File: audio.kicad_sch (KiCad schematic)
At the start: 109 parts, among them IC201 LC7881M, IC202 RC4560, IC203 RC4558, IC204 RC4558, J1 0, J2 0, Q201 2SC2412K, Q202 2SC2412K, Q203 DTA124EU3, Q204 DTA124EU3, Q205 Q_NPN_BEC, Q206 Q_NPN_BEC, Q207 DTC114EU3, Q208 Q_NPN_BEC, Q209 Q_NPN_BEC, Q302 2SC2412K, Q307 2SC2412K, Q601 Q_NPN_BEC, Q602 Q_NPN_BEC

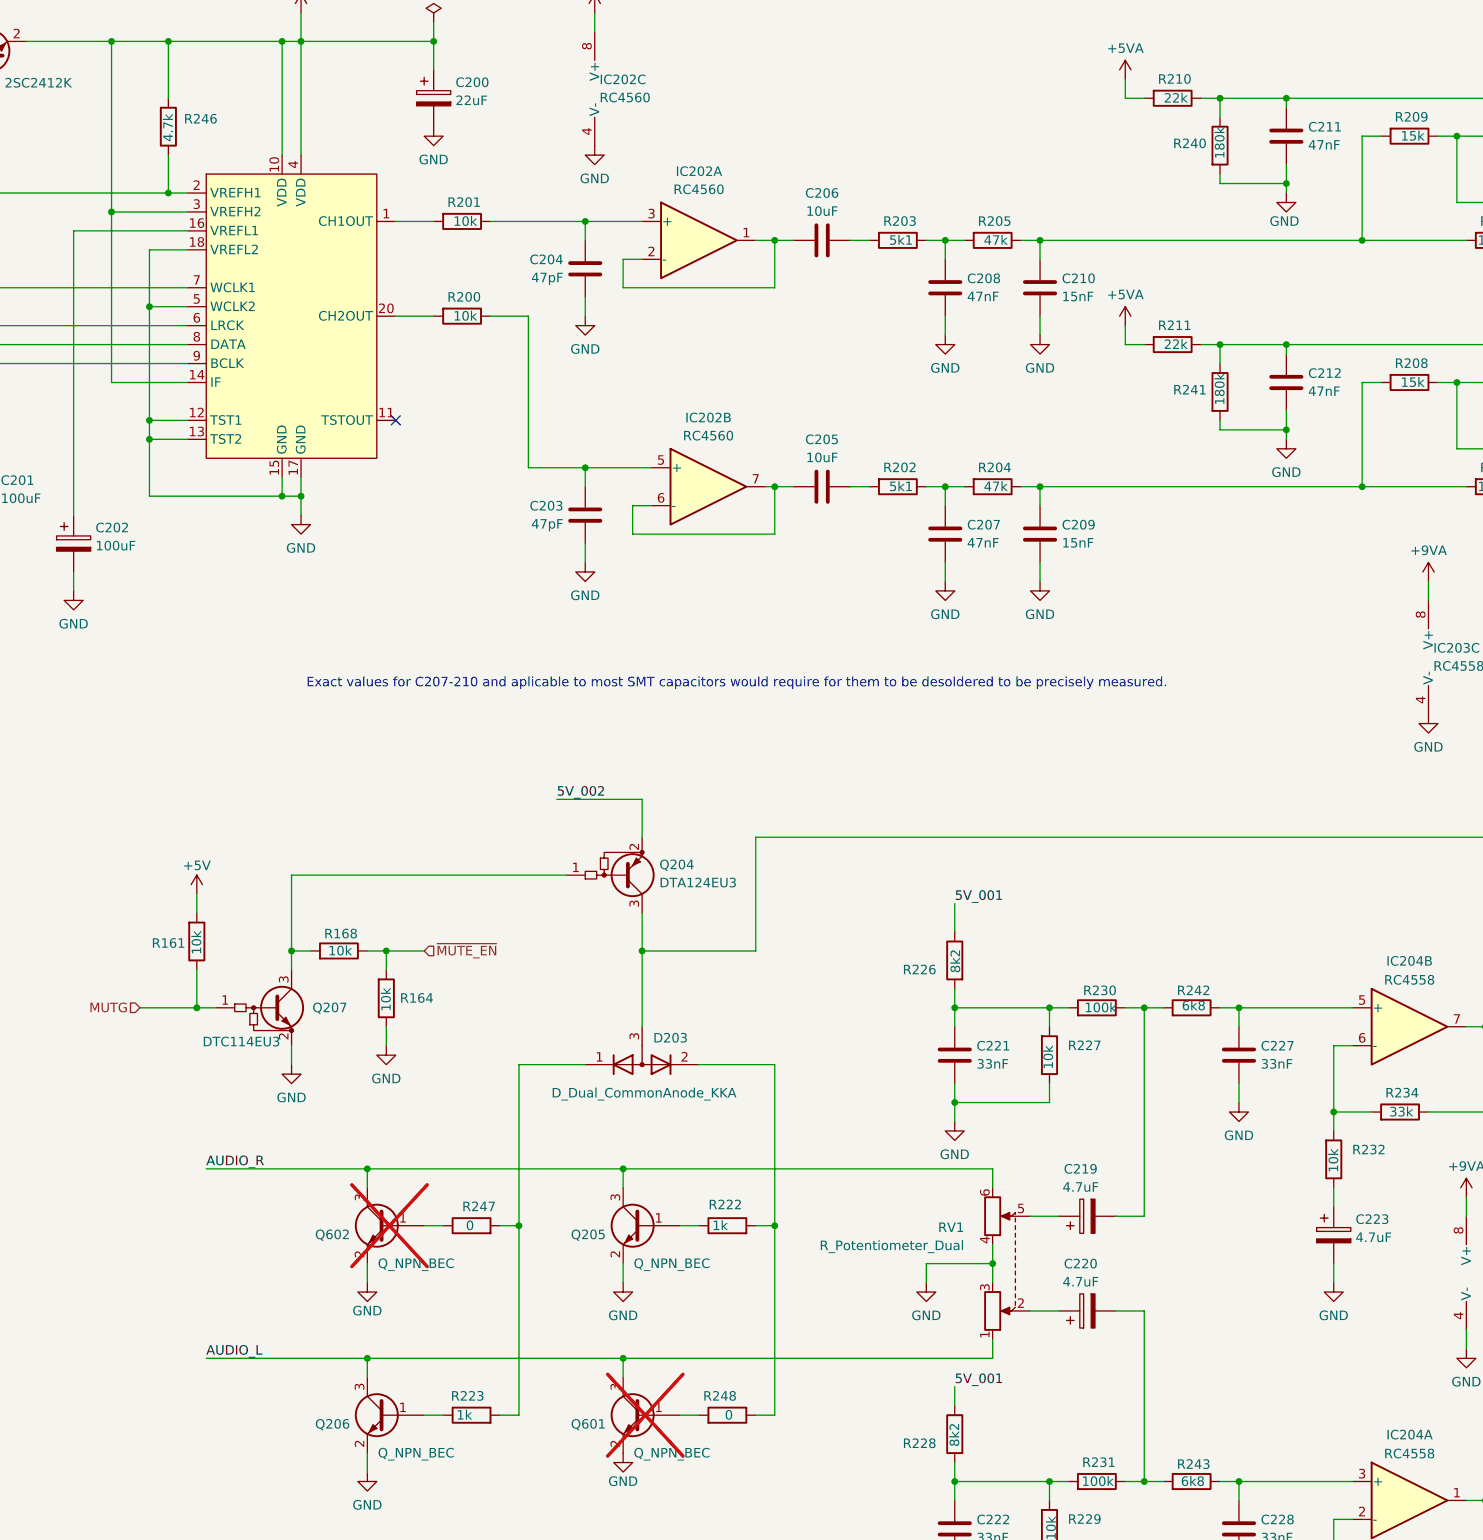
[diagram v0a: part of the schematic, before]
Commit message: Small Schematics update to tidy signals attached to SCSI and MCU chips.
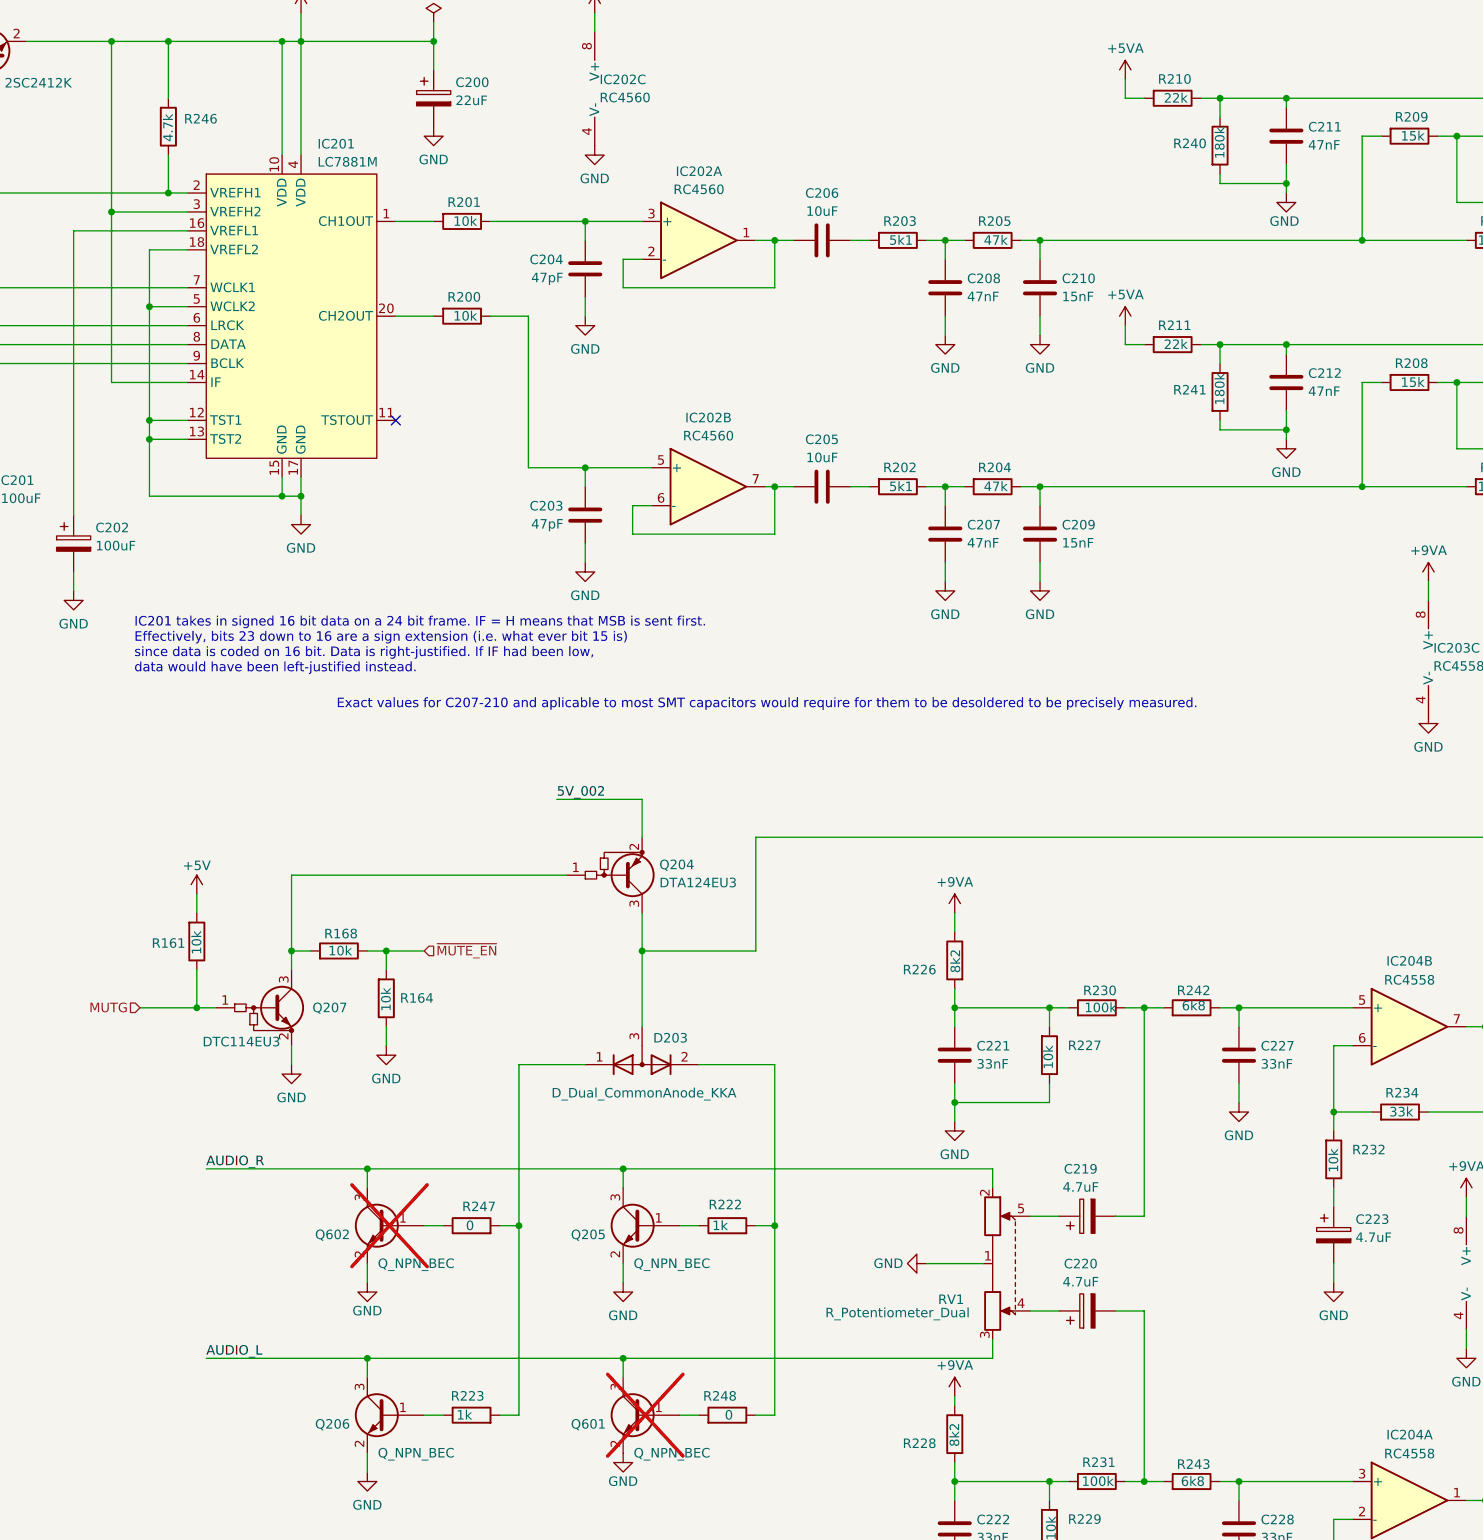
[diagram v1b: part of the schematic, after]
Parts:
- RV1: symbol Device:R_Potentiometer_Dual -> PC-Engine_CDR-30:R_Potentiometer_Dual
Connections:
- net 5V_001 is gone; now on net +9VA: R226.1, R228.1
- net AUDIO_L: now also RV1.3; no longer RV1.1
- net AUDIO_R: now also RV1.2; no longer RV1.6
- net GND: now also RV1.1; no longer RV1.3, RV1.4
- net at C220.1: now also RV1.4; no longer RV1.2
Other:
- note added: "IC201 takes in signed 16 bit data on a 24 bit frame. IF = H means that MSB is sent first. Effectively, bits 23 down to 16 are a sign extension (i.e. what ever bit 15 is) since data is coded on 16 bit. Data is right-justified. If IF had been low, data would have been left-justified instead."
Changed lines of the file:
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@@
 	(title_block
 		(title "PC-Engine CDR-30A (CD-ROM2) Schematics - MAIN PWR")
-		(date "2024-05-03")
-		(rev "0.1")
+		(date "2024-07-19")
+		(rev "0.2")
 		(company "Author: Regis Galland")
 	)
@@
 	)
 	(junction
-		(at 170.18 189.23)
-		(diameter 0)
-		(color 0 0 0 0)
-	)
-	(junction
 		(at 254 46.99)
 		(diameter 0)
@@
 	(wire
 		(pts
-			(xy 165.1 205.74) (xy 165.1 208.28)
+			(xy 165.1 207.01) (xy 165.1 208.28)
 		)
 		(stroke
@@
 	(wire
 		(pts
-			(xy 165.1 140.97) (xy 165.1 144.78)
+			(xy 165.1 142.24) (xy 165.1 144.78)
 		)
 		(stroke
@@
 	(wire
 		(pts
-			(xy 170.18 186.69) (xy 170.18 189.23)
-		)
-		(stroke
-			(width 0)
-			(type default)
-		)
-	)
-	(wire
-		(pts
 			(xy 342.9 71.12) (xy 342.9 73.66)
 		)
@@
 	(wire
 		(pts
-			(xy 170.18 189.23) (xy 170.18 191.77)
-		)
-		(stroke
-			(width 0)
-			(type default)
-		)
-	)
-	(wire
-		(pts
 			(xy 254 68.58) (xy 254 80.01)
 		)
@@
 	(wire
 		(pts
-			(xy 161.29 189.23) (xy 161.29 191.77)
-		)
-		(stroke
-			(width 0)
-			(type default)
-		)
-	)
-	(wire
-		(pts
 			(xy 365.76 66.04) (xy 365.76 99.06)
 		)
@@
 	(wire
 		(pts
-			(xy 161.29 189.23) (xy 170.18 189.23)
+			(xy 161.29 189.23) (xy 168.91 189.23)
 		)
 		(stroke
@@
 		)
 	)
+	(text "IC201 takes in signed 16 bit data on a 24 bit frame. IF = H means that MSB is sent first.\nEffectively, bits 23 down to 16 are a sign extension (i.e. what ever bit 15 is) \nsince data is coded on 16 bit. Data is right-justified. If IF had been low,\ndata would have been left-justified instead."
+		(exclude_from_sim no)
+		(at 55.118 106.426 0)
+		(effects
+			(font
+				(size 1.27 1.27)
+			)
+			(justify left)
+		)
+	)
 	(text "LINE OUT"
 		(exclude_from_sim no)
@@
 	(text "Exact values for C207-210 and aplicable to most SMT capacitors would require for them to be desoldered to be precisely measured."
 		(exclude_from_sim no)
-		(at 135.89 111.506 0)
+		(at 139.954 114.3 0)
 		(effects
 			(font
@@
 		)
 	)
-	(label "5V_001"
-		(at 165.1 205.74 0)
-		(fields_autoplaced yes)
-		(effects
-			(font
-				(size 1.27 1.27)
-			)
-			(justify left bottom)
-		)
-	)
 	(label "AUDIO_L"
 		(at 314.96 68.58 180)
@@
 		)
 	)
-	(label "5V_001"
-		(at 165.1 140.97 0)
-		(fields_autoplaced yes)
-		(effects
-			(font
-				(size 1.27 1.27)
-			)
-			(justify left bottom)
-		)
-	)
 	(label "5V_002"
 		(at 111.76 127 0)
@@
 	)
 	(symbol
-		(lib_id "Device:R_Potentiometer_Dual")
+		(lib_id "PC-Engine_CDR-30:R_Potentiometer_Dual")
 		(at 172.72 189.23 270)
-		(mirror x)
 		(unit 1)
 		(exclude_from_sim no)
@@
 		(dnp no)
 		(property "Reference" "RV1"
-			(at 166.37 184.404 90)
+			(at 166.37 194.056 90)
 			(effects
 				(font
@@
 		)
 		(property "Value" "R_Potentiometer_Dual"
-			(at 166.37 186.8283 90)
+			(at 167.132 195.834 90)
 			(effects
 				(font
@@
 		)
 		(property "Footprint" ""
-			(at 170.815 182.88 0)
+			(at 170.815 195.58 0)
 			(effects
 				(font
@@
 		)
 		(property "Datasheet" "~"
-			(at 170.815 182.88 0)
+			(at 170.815 195.58 0)
 			(effects
 				(font
@@
 		)
 		(property "Description" "Dual potentiometer"
-			(at 172.72 189.23 0)
+			(at 164.592 188.468 0)
 			(effects
 				(font
@@
 		(pin "1"
 		)
-		(pin "6"
-		)
 		(pin "4"
 		)
@@
 	)
 	(symbol
+		(lib_id "power:+9VA")
+		(at 165.1 207.01 0)
+		(unit 1)
+		(exclude_from_sim no)
+		(in_bom yes)
+		(on_board yes)
+		(dnp no)
+		(fields_autoplaced yes)
+		(property "Reference" "#PWR095"
+			(at 165.1 210.185 0)
+			(effects
+				(font
+					(size 1.27 1.27)
+				)
+				(hide yes)
+			)
+		)
+		(property "Value" "+9VA"
+			(at 165.1 202.8769 0)
+			(effects
+				(font
+					(size 1.27 1.27)
+				)
+			)
+		)
+		(property "Footprint" ""
+			(at 165.1 207.01 0)
+			(effects
+				(font
+					(size 1.27 1.27)
+				)
+				(hide yes)
+			)
+		)
+		(property "Datasheet" ""
+			(at 165.1 207.01 0)
+			(effects
+				(font
+					(size 1.27 1.27)
+				)
+				(hide yes)
+			)
+		)
+		(property "Description" "Power symbol creates a global label with name \"+9VA\""
+			(at 165.1 207.01 0)
+			(effects
+				(font
+					(size 1.27 1.27)
+				)
+				(hide yes)
+			)
+		)
+		(pin "1"
+		)
+		(instances
+			(project "MAIN_PWR"
+				(path "/035ab33a-1caf-4155-b57e-664ce0b37194/c66865a7-8f9d-4776-b068-2ea23e8097e3"
+					(reference "#PWR095")
+					(unit 1)
+				)
+			)
+		)
+	)
+	(symbol
 		(lib_id "Device:R")
 		(at 157.48 85.09 270)
@@
 	(symbol
 		(lib_id "power:GND")
-		(at 161.29 191.77 0)
+		(at 161.29 189.23 270)
 		(unit 1)
 		(exclude_from_sim no)
@@
 		(on_board yes)
 		(dnp no)
-		(fields_autoplaced yes)
 		(property "Reference" "#PWR045"
-			(at 161.29 198.12 0)
+			(at 154.94 189.23 0)
 			(effects
 				(font
@@
 		)
 		(property "Value" "GND"
-			(at 161.29 196.2134 0)
+			(at 156.21 189.23 90)
 			(effects
 				(font
@@
 		)
 		(property "Footprint" ""
-			(at 161.29 191.77 0)
+			(at 161.29 189.23 0)
 			(effects
 				(font
@@
 		)
 		(property "Datasheet" ""
-			(at 161.29 191.77 0)
+			(at 161.29 189.23 0)
 			(effects
 				(font
@@
 		)
 		(property "Description" "Power symbol creates a global label with name \"GND\" , ground"
-			(at 161.29 191.77 0)
+			(at 161.29 189.23 0)
 			(effects
 				(font
@@
 	)
 	(symbol
+		(lib_id "power:+9VA")
+		(at 165.1 142.24 0)
+		(unit 1)
+		(exclude_from_sim no)
+		(in_bom yes)
+		(on_board yes)
+		(dnp no)
+		(fields_autoplaced yes)
+		(property "Reference" "#PWR094"
+			(at 165.1 145.415 0)
+			(effects
+				(font
+					(size 1.27 1.27)
+				)
+				(hide yes)
+			)
+		)
+		(property "Value" "+9VA"
+			(at 165.1 138.1069 0)
+			(effects
+				(font
+					(size 1.27 1.27)
+				)
+			)
+		)
+		(property "Footprint" ""
+			(at 165.1 142.24 0)
+			(effects
+				(font
+					(size 1.27 1.27)
+				)
+				(hide yes)
+			)
+		)
+		(property "Datasheet" ""
+			(at 165.1 142.24 0)
+			(effects
+				(font
+					(size 1.27 1.27)
+				)
+				(hide yes)
+			)
+		)
+		(property "Description" "Power symbol creates a global label with name \"+9VA\""
+			(at 165.1 142.24 0)
+			(effects
+				(font
+					(size 1.27 1.27)
+				)
+				(hide yes)
+			)
+		)
+		(pin "1"
+		)
+		(instances
+			(project "MAIN_PWR"
+				(path "/035ab33a-1caf-4155-b57e-664ce0b37194/c66865a7-8f9d-4776-b068-2ea23e8097e3"
+					(reference "#PWR094")
+					(unit 1)
+				)
+			)
+		)
+	)
+	(symbol
 		(lib_id "power:GND")
 		(at 165.1 170.18 0)
@@
 				)
 				(justify left)
-				(hide yes)
 			)
 		)
@@
 				)
 				(justify left)
-				(hide yes)
 			)
 		)

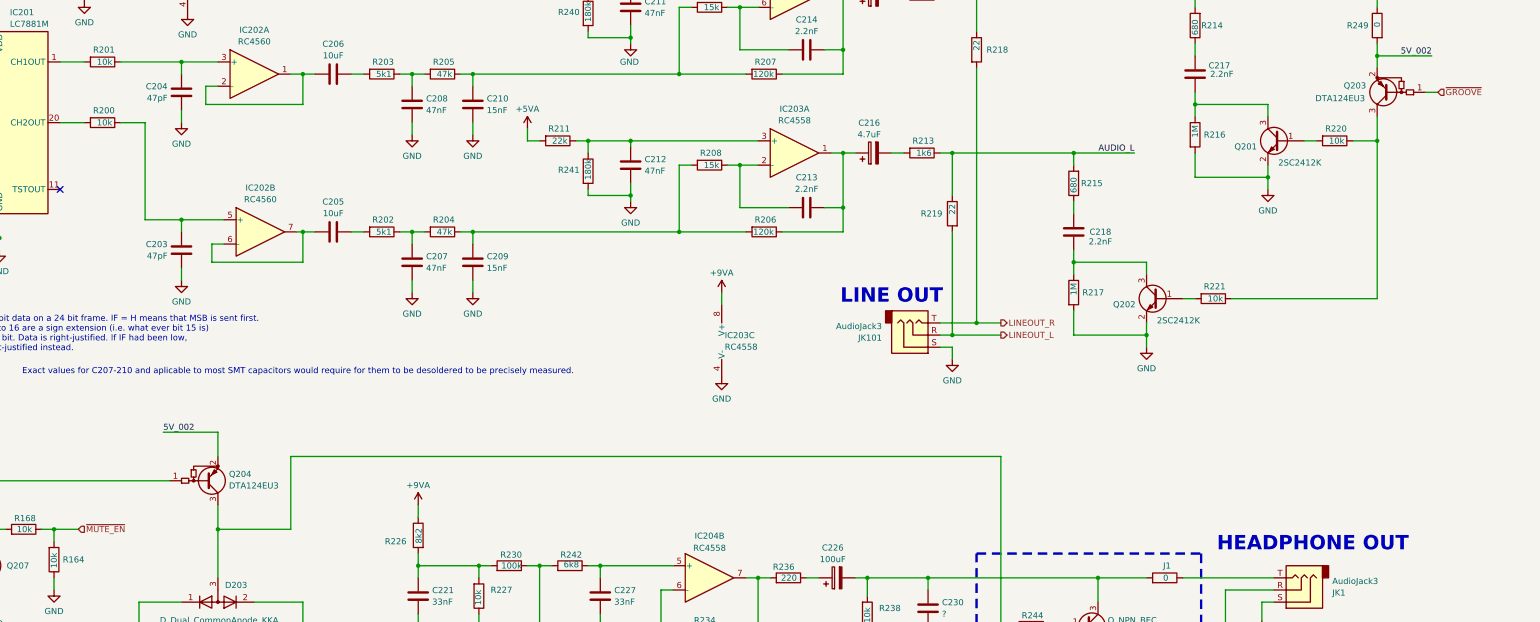
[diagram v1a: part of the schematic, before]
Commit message: Small update, some typo fixes, more comments added to help understanding
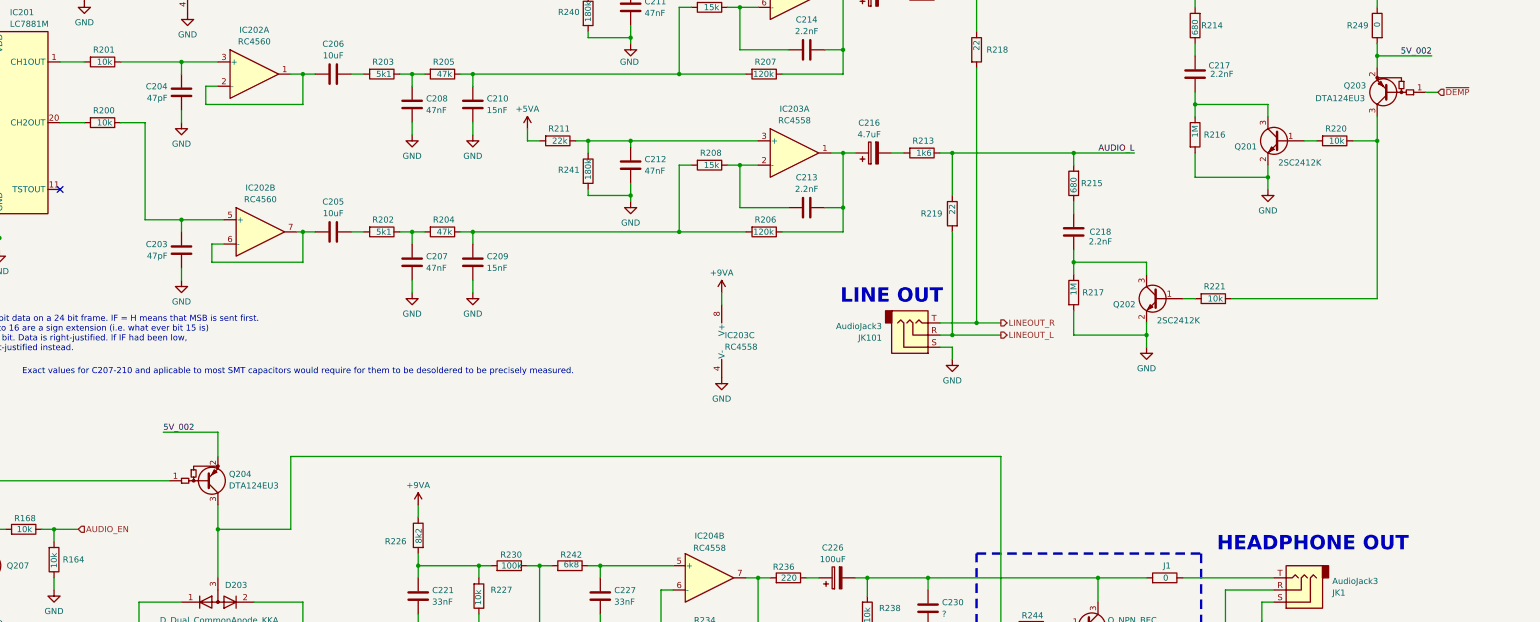
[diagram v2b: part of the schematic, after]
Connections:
- net ~{GROOVE} renamed ~{DEMP}
- net ~{MUTE_EN} renamed AUDIO_EN
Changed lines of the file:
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@@
 		)
 	)
-	(hierarchical_label "~{MUTE_EN}"
+	(hierarchical_label "AUDIO_EN"
 		(shape input)
 		(at 93.98 147.32 0)
@@
 		)
 	)
-	(hierarchical_label "~{GROOVE}"
+	(hierarchical_label "~{DEMP}"
 		(shape input)
 		(at 378.46 55.88 0)
